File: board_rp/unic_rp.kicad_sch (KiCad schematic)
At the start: 207 parts, among them J2 USB_C_Receptacle, Q1 2N7002, Q10 2N7002, Q11 2N7002, Q12 2N7002, Q13 2N7002, Q14 2N7002, Q15 2N7002, Q16 2N7002, Q17 2N7002, Q18 2N7002, Q19 2N7002, Q2 2N7002, Q20 2N7002, Q21 2N7002, Q22 2N7002, Q23 2N7002, Q24 2N7002, Q25 2N7002, Q26 2N7002, Q27 2N7002, Q28 2N7002, Q29 2N7002, Q3 2N7002, Q30 2N7002, Q31 2N7002, Q32 2N7002, Q33 2N7002, Q34 2N7002, Q35 2N7002, Q36 2N7002, Q37 2N7002, Q38 2N7002, Q39 2N7002, Q4 2N7002, Q40 2N7002, Q41 2N7002, Q42 AO3401A, Q43 2N7002, Q5 2N7002, Q6 2N7002, Q7 2N7002, Q8 2N7002, Q9 2N7002, U1 RP2350_80QFN, U10 ESD224DQA, U2 ESD224DQA, U3 MIC5203-3.3BM5, U4 APS6404L-3SQR-ZR, U5 TMUX154ERSW, U6 AP62150Z6, U7 W25Q16JVUXIQ, U8 LM393, U9 74AUP1G08, X1 27MHz

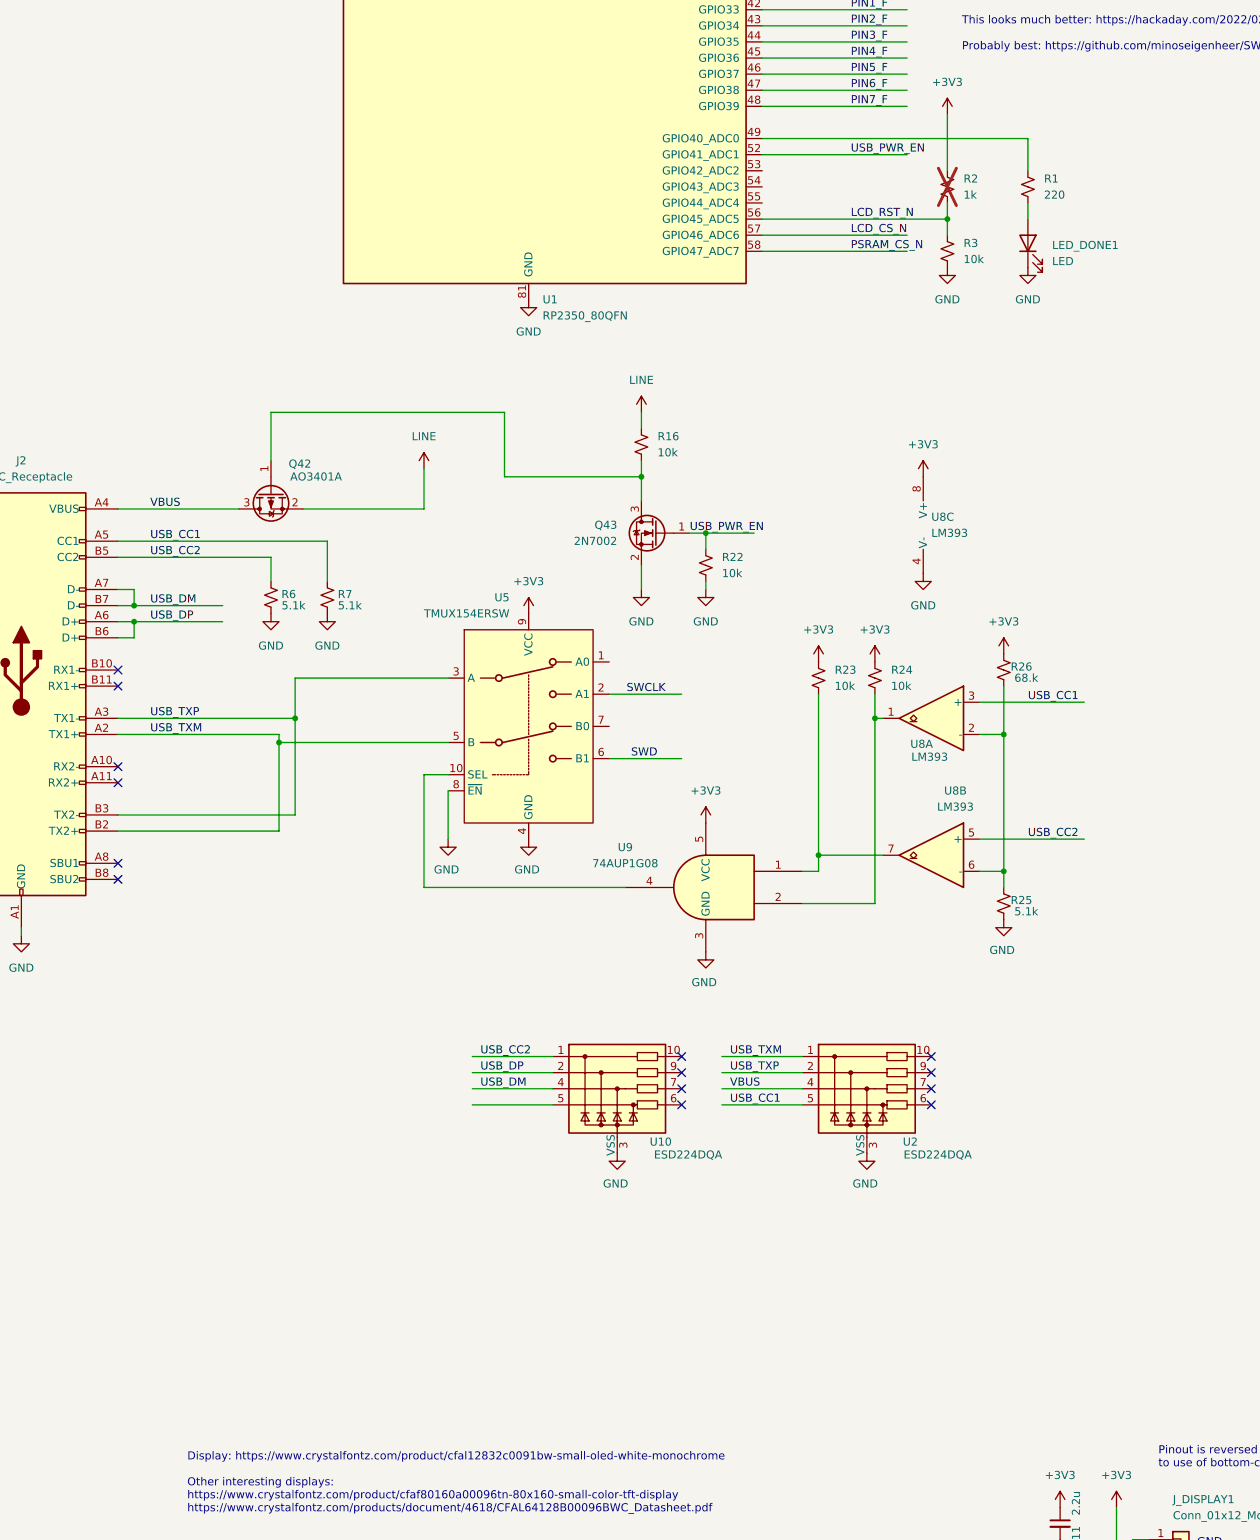
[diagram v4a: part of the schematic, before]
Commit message: More or less complete schematic.
Component selection is not final, but functionality around
USB-C connector is. We even have UART output on it now as
well as USB VBUS detection and control on the right pins.
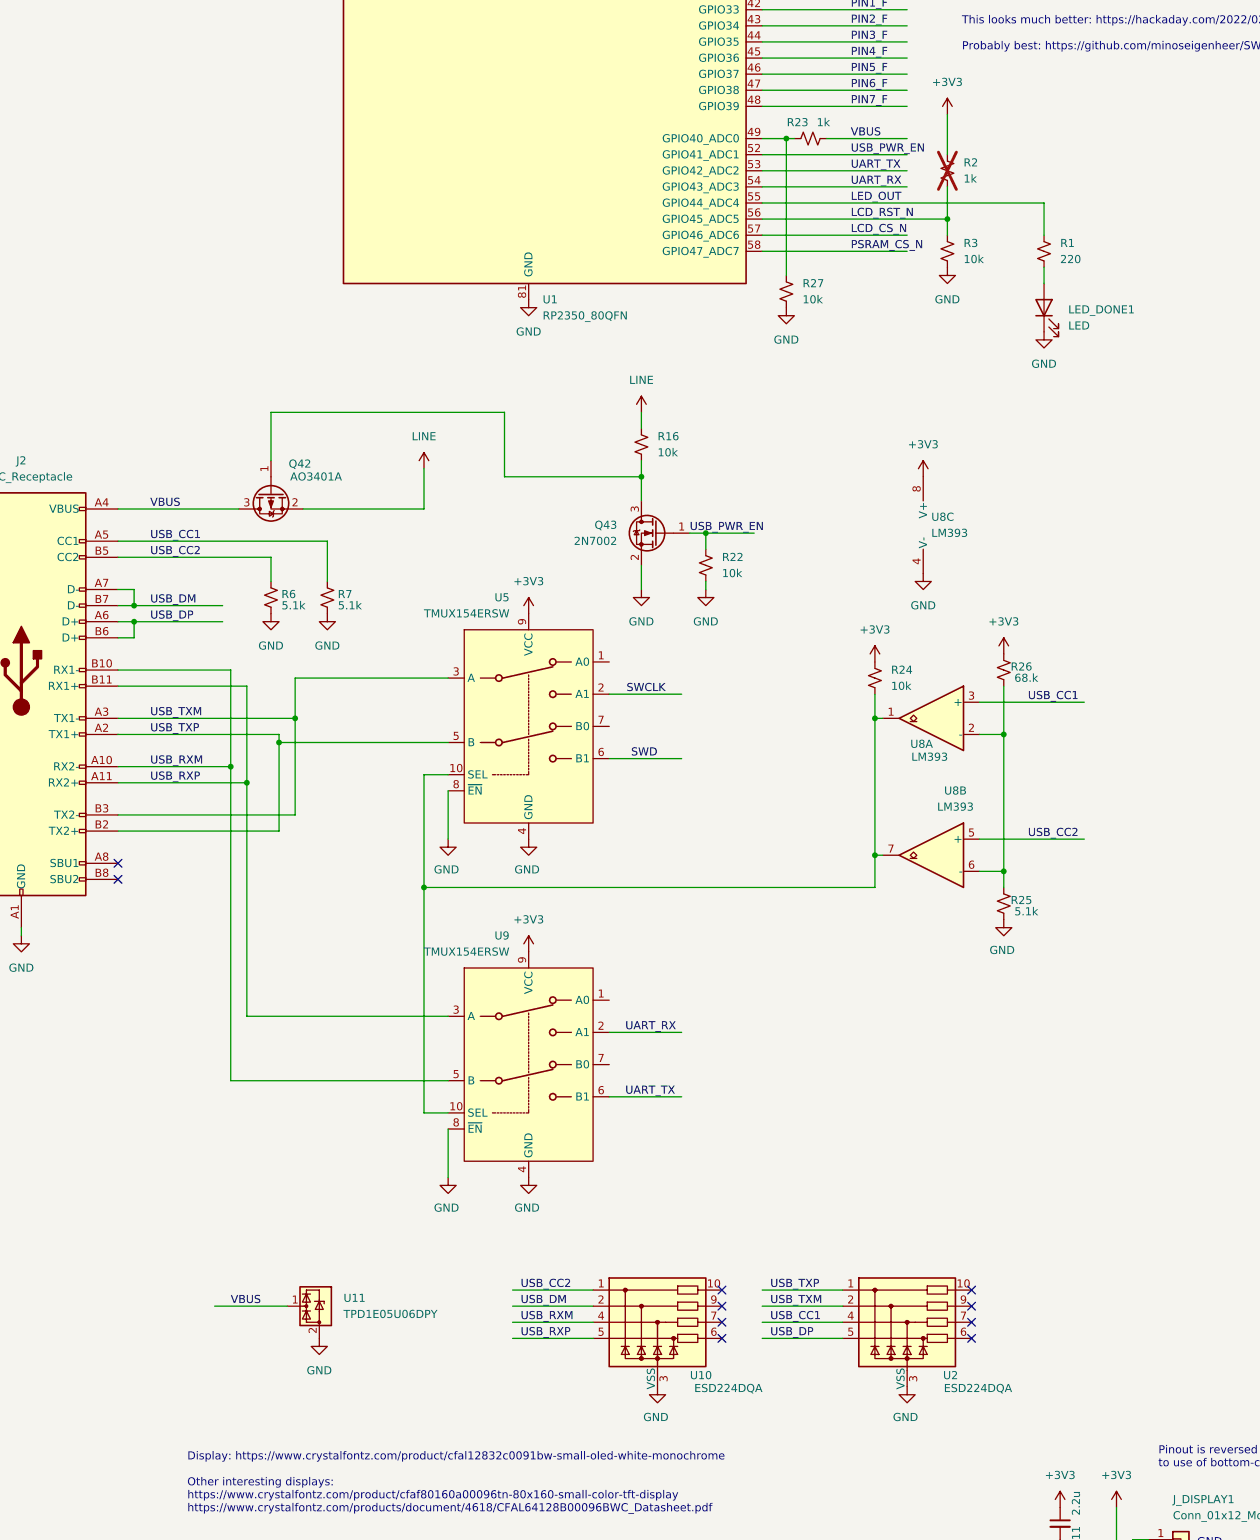
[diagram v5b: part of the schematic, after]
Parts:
- removed U9: 74AUP1G08, Package_TO_SOT_SMD:SOT-353_SC-70-5, symbol 74xGxx:74AUP1G08
- added R27: 10k, UNIC:R_0402_1005Metric_Pad0.72x0.64mm_HandSolder, symbol Device:R_Small_US
- added U11: TPD1E05U06DPY, Package_SON:Texas_DPY0002A_0.6x1mm_P0.65mm, symbol Power_Protection:TPD1E05U06DPY
- added U9: TMUX154ERSW, Package_DFN_QFN:UQFN-10_1.4x1.8mm_P0.4mm, symbol Analog_Switch:TMUX154ERSW
- R23: value 10k -> 1k; mpn CR0402-FX-1002GLF -> CR0402-JW-102GLF
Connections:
- net +3V3: now also U9.9 (VCC); no longer R23.1
- net GND: now also R27.2, U11.2 (GND), U9.4 (GND), U9.8 (~{EN})
- net USB_CC1: now also U2.4; no longer U2.5
- net USB_DM: now also U10.2; no longer U10.4
- net USB_DP: now also U2.5; no longer U10.2
- net USB_TXM: now also J2.A3 (TX1-), J2.B3 (TX2-), U2.2, U5.3 (A); no longer J2.A2 (TX1+), J2.B2 (TX2+), U2.1, U5.5 (B)
- net USB_TXP: now also J2.A2 (TX1+), J2.B2 (TX2+), U2.1, U5.5 (B); no longer J2.A3 (TX1-), J2.B3 (TX2-), U2.2, U5.3 (A)
- net VBUS: now also R23.2, U11.1 (I/O); no longer U2.4
- net at U5.10 (SEL): now also R24.2, U8.1, U8.7, U9.10 (SEL)
- net USB_RXP: now reaches U10.5
- net USB_RXP: now also J2.A11 (RX2+), J2.B11 (RX1+), U9.3 (A)
- net USB_RXM: now reaches J2.A10 (RX2-)
- net USB_RXM: now also J2.B10 (RX1-), U10.4, U9.5 (B)
- net at U1.49 (GPIO40_ADC0): now also R23.1, R27.1; no longer R1.1
- net UART_TX: now reaches U1.53 (GPIO42_ADC2)
- net UART_TX: now also U9.6 (B1)
- net UART_RX: now reaches U1.54 (GPIO43_ADC3)
- net UART_RX: now also U9.2 (A1)
- net LED_OUT: now reaches U1.55 (GPIO44_ADC4)
- net LED_OUT: now also R1.1
- no-connect marks 17 -> 13
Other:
- moved on the sheet: LED_DONE1, R1, R2, U10, U2

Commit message: Component selection I think now is complete.
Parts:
- removed U11: TPD1E05U06DPY, Package_SON:Texas_DPY0002A_0.6x1mm_P0.65mm, symbol Power_Protection:TPD1E05U06DPY
- removed U5, U9: TMUX154ERSW, Package_DFN_QFN:UQFN-10_1.4x1.8mm_P0.4mm, symbol Analog_Switch:TMUX154ERSW
- removed X1: 27MHz, UNIC:Oscillator_SMD_Abracon_ASE-4Pin_3.2x2.5mm, symbol Oscillator:ASE-xxxMHz
- added C2, C25: 15p, UNIC:C_0402_1005Metric_Pad0.74x0.62mm_HandSolder, symbol Device:C_Small
- added D21: PESD5V0L1BSLAZ, UNIC:D_SOD-882, symbol Diode:ESD9B5.0ST5G
- added U12: 4066, Package_DFN_QFN:DHVQFN-14-1EP_2.5x3mm_P0.5mm_EP1x1.5mm, symbol 4xxx:4066
- added Y1: 12MHz, UNIC:Oscillator_SMD_Abracon_ASE-4Pin_3.2x2.5mm, symbol Device:Crystal_GND24
- L2: mpn (none) -> WIP201610S-4R7MLDG
- U10, U2: mpn (none) -> TVU1240R1ADG
- U6: value AP62150Z6 -> TPS562242DRLR
- U8: footprint Package_SON:WSON-8-1EP_3x2.5mm_P0.5mm_EP1.2x1.5mm_PullBack -> Package_SON:WSON-8-1EP_2x2mm_P0.5mm_EP0.9x1.6mm; symbol Comparator:LM393 -> UNIC:LM393; mpn (none) -> LM393BIDSGR
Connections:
- net +3V3: now also U12.14 (VDD)
- net CLK1: now also C2.1, Y1.1
- net GND: now also U8.9 (PAD), C2.2, C25.2, D21.1 (A1), U12.7 (VSS)
- net SWCLK: now also U12.2
- net SWD: now also U12.3
- net UART_RX: now also U12.9
- net UART_TX: now also U12.11
- net USB_RXM: now also U12.10
- net USB_RXP: now also U12.8
- net USB_TXM: now also U12.1
- net USB_TXP: now also U12.4
- net VBUS: now also D21.2 (A2)
- net at R24.2, U8.1, U8.7: now also U12.12, U12.13, U12.5, U12.6
- net at U1.31 (XOUT): now also C25.1, Y1.3
- no-connect marks 13 -> 12
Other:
- note added: "Follwing the lead of: https://github.com/minoseigenheer/SWD-over-USB-C"
- note added: "TODO: review and update to cheap OLED footprint. Might need different connector too."
- note removed: "ECO: change part to TPS562242"
- note removed: "Even though we could sustain the I/O current through an LDO, the SDRAM consumes and extra 80mA or so. Better use a switcher for 3.3V."
- note removed: "NOT SURE HOW TO IMPLEMENT SWI OVER USB OR HOW TO DETECT WHEN TO SUPPLY POWER (OTG?) Someone thought of this already: https://hackaday.io/project/192857-swd-over-usb-type-c-new-way-of-programming-boards Looks sketchy though... This looks much better: https://hackaday.com/2022/02/24/an-unbusy-usb-c-port-doubles-up-for-jtag-programming/ Probably best: https://github.com/minoseigenheer/SWD-over-USB-C"
- note removed: "TODO: make sure LCD can be connected to normal SPI, if not, switch to I2C"
- moved on the sheet: U10, U2

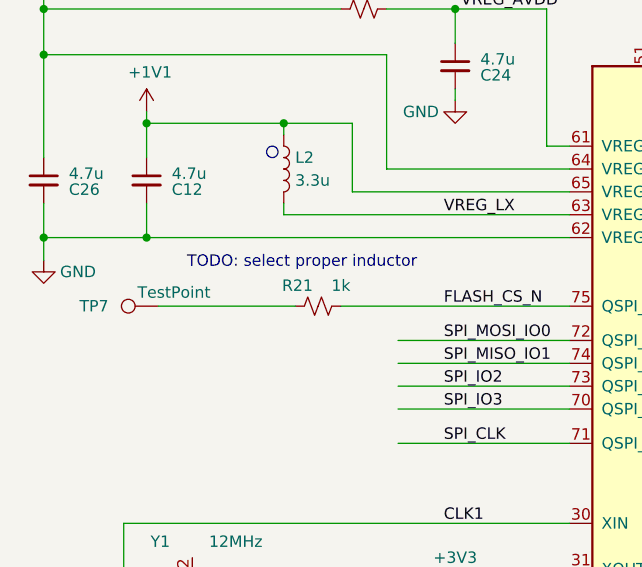
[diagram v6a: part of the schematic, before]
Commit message: More or less complete routing.
There are a few clearance violations with NPTH that doesn't
make sense. Also, power planes are not in yet, only wires.
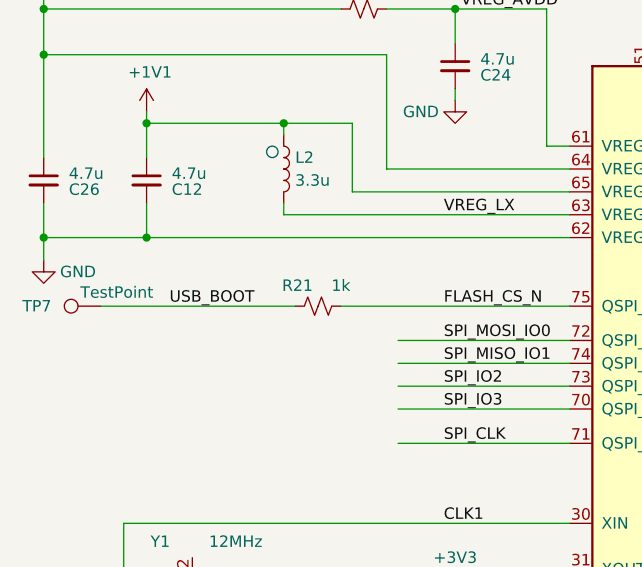
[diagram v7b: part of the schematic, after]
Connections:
- net USB_BOOT: now reaches R21.1, TP7.1
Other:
- note removed: "TODO: select proper inductor"
- moved on the sheet: TP7
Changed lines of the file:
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@@
 	(wire
 		(pts
-			(xy 33.02 59.69) (xy 48.26 59.69)
+			(xy 26.67 59.69) (xy 48.26 59.69)
 		)
 		(stroke
@@
 		)
 	)
-	(text "TODO: select proper inductor"
-		(exclude_from_sim no)
-		(at 49.022 54.864 0)
-		(effects
-			(font
-				(size 1.27 1.27)
-			)
-		)
-	)
 	(text "RES#"
 		(exclude_from_sim no)
@@
 		)
 	)
+	(label "USB_BOOT"
+		(at 34.29 59.69 0)
+		(fields_autoplaced yes)
+		(effects
+			(font
+				(size 1.27 1.27)
+			)
+			(justify left bottom)
+		)
+	)
 	(label "SPI_CLK"
 		(at 64.77 74.93 0)
@@
 	(symbol
 		(lib_id "Connector:TestPoint")
-		(at 33.02 59.69 90)
+		(at 26.67 59.69 90)
 		(unit 1)
 		(exclude_from_sim no)
@@
 		(dnp no)
 		(property "Reference" "TP7"
-			(at 25.908 59.69 90)
+			(at 19.558 59.69 90)
 			(effects
 				(font
@@
 		)
 		(property "Value" "TestPoint"
-			(at 34.798 58.166 90)
+			(at 28.448 58.166 90)
 			(effects
 				(font
@@
 		)
 		(property "Footprint" "UNIC:TestPoint_Pad_D2.0mm"
-			(at 33.02 54.61 0)
+			(at 26.67 54.61 0)
 			(effects
 				(font
@@
 		)
 		(property "Datasheet" "~"
-			(at 33.02 54.61 0)
+			(at 26.67 54.61 0)
 			(effects
 				(font
@@
 		)
 		(property "Description" "test point"
-			(at 33.02 59.69 0)
+			(at 26.67 59.69 0)
 			(effects
 				(font
@@
 		)
 		(property "manf" ""
-			(at 33.02 59.69 0)
+			(at 26.67 59.69 0)
 			(effects
 				(font
@@
 		)
 		(property "manf#" ""
-			(at 33.02 59.69 0)
+			(at 26.67 59.69 0)
 			(effects
 				(font
@@
 		)
 		(property "MP" ""
-			(at 33.02 59.69 0)
+			(at 26.67 59.69 0)
 			(effects
 				(font
@@
 		)
 		(property "SnapEDA_Link" ""
-			(at 33.02 59.69 0)
+			(at 26.67 59.69 0)
 			(effects
 				(font

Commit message: Much UnIC RP cleanup.
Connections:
- net UART_RX: now also U12.11; no longer U12.9
- net UART_TX: now also U12.9; no longer U12.11
- net USB_RXM: now also U12.8; no longer U12.10
- net USB_RXP: now also U12.10; no longer U12.8
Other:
- moved on the sheet: U12C, U12D
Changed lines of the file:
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@@
 	(symbol
 		(lib_id "4xxx:4066")
-		(at 115.57 297.18 0)
+		(at 105.41 284.48 0)
 		(mirror y)
 		(unit 4)
@@
 		(dnp no)
 		(property "Reference" "U12"
-			(at 115.57 302.26 0)
+			(at 105.41 289.56 0)
 			(effects
 				(font
@@
 		)
 		(property "Value" "4066"
-			(at 115.57 304.8 0)
+			(at 105.41 292.1 0)
 			(effects
 				(font
@@
 		)
 		(property "Footprint" "Package_DFN_QFN:DHVQFN-14-1EP_2.5x3mm_P0.5mm_EP1x1.5mm"
-			(at 115.57 297.18 0)
+			(at 105.41 284.48 0)
 			(effects
 				(font
@@
 		)
 		(property "Datasheet" "https://assets.nexperia.com/documents/data-sheet/74HC_HCT4066.pdf"
-			(at 115.57 297.18 0)
+			(at 105.41 284.48 0)
 			(effects
 				(font
@@
 		)
 		(property "Description" "Quad Analog Switches"
-			(at 115.57 297.18 0)
+			(at 105.41 284.48 0)
 			(effects
 				(font
@@
 		)
 		(property "mpn" "74HC4066BQ,115"
-			(at 115.57 297.18 0)
+			(at 105.41 284.48 0)
 			(effects
 				(font
@@
 	(symbol
 		(lib_id "4xxx:4066")
-		(at 105.41 284.48 0)
+		(at 115.57 297.18 0)
 		(unit 3)
 		(exclude_from_sim no)
@@
 		(fields_autoplaced yes)
 		(property "Reference" "U12"
-			(at 105.41 289.56 0)
+			(at 115.57 302.26 0)
 			(effects
 				(font
@@
 		)
 		(property "Value" "4066"
-			(at 105.41 292.1 0)
+			(at 115.57 304.8 0)
 			(effects
 				(font
@@
 		)
 		(property "Footprint" "Package_DFN_QFN:DHVQFN-14-1EP_2.5x3mm_P0.5mm_EP1x1.5mm"
-			(at 105.41 284.48 0)
+			(at 115.57 297.18 0)
 			(effects
 				(font
@@
 		)
 		(property "Datasheet" "https://assets.nexperia.com/documents/data-sheet/74HC_HCT4066.pdf"
-			(at 105.41 284.48 0)
+			(at 115.57 297.18 0)
 			(effects
 				(font
@@
 		)
 		(property "Description" "Quad Analog Switches"
-			(at 105.41 284.48 0)
+			(at 115.57 297.18 0)
 			(effects
 				(font
@@
 		)
 		(property "mpn" "74HC4066BQ,115"
-			(at 105.41 284.48 0)
+			(at 115.57 297.18 0)
 			(effects
 				(font
